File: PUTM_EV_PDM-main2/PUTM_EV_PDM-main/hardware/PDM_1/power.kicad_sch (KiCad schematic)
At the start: 20 parts, among them U2 LD1117S33TR_SOT223, U3 LM2675M-5

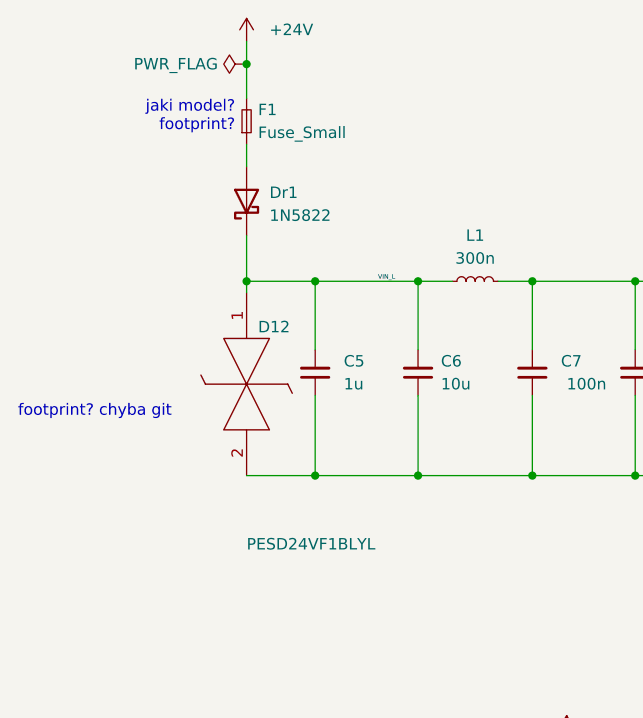
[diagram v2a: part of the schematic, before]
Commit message: małe zmiany
dodano złącza
zmieniono parę footprintów
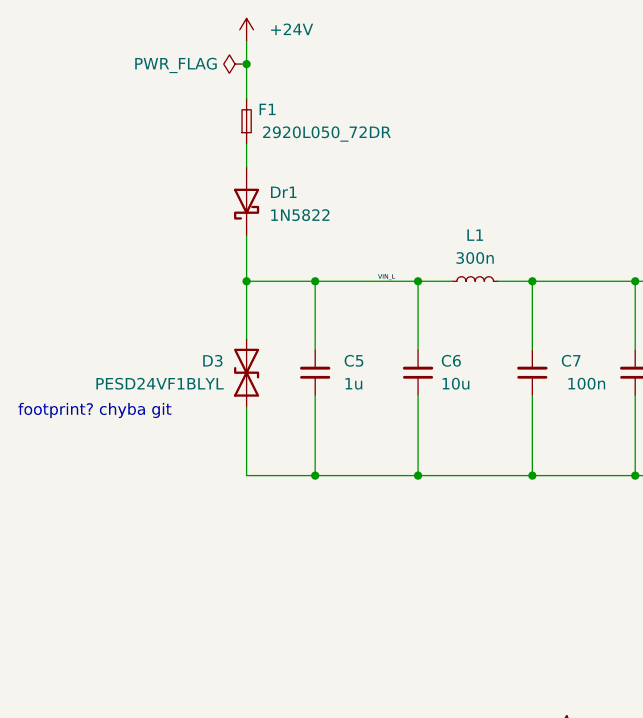
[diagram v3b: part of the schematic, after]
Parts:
- removed D12: PESD24VF1BLYL, Diode_SMD:D_SMA, symbol PESD24VF1BLYL:PESD24VF1BLYL
- added D3: PESD24VF1BLYL, Diode_SMD:D_SMA, symbol Device:D_TVS
- C14: footprint Capacitor_SMD:CP_Elec_6.3x5.5 -> Capacitor_SMD:CP_Elec_6.3x5.4
- F1: value Fuse_Small -> 2920L050_72DR; footprint (none) -> FUSC7451X125N; Height (none) -> 1.25; Manufacturer_Name (none) -> LITTELFUSE; Manufacturer_Part_Number (none) -> 2920L050/72DR; Mouser Part Number (none) -> 576-2920L050/72DR; Mouser Price/Stock (none) -> https://www.mouser.co.uk/ProductDetail/Littelfuse/2920L050-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
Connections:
- net GND: now also D3.1 (A1)
- net VIN_L: now also D3.2 (A2)
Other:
- note removed: "jaki model? footprint?"
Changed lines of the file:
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@@
     (stroke (width 0) (type default))
   )
-  (wire (pts (xy 76.2 77.47) (xy 76.2 78.74))
+  (wire (pts (xy 76.2 77.47) (xy 76.2 83.82))
     (stroke (width 0) (type default))
   )
   (wire (pts (xy 119.38 77.47) (xy 129.54 77.47))
+    (stroke (width 0) (type default))
+  )
+  (wire (pts (xy 76.2 91.44) (xy 76.2 99.06))
     (stroke (width 0) (type default))
   )
@@
   (text "footprint? chyba git" (at 50.8 92.71 0)
     (effects (font (size 1.27 1.27)) (justify left bottom))
-  )
-  (text "jaki model?\nfootprint?\n" (at 74.93 60.96 0)
-    (effects (font (size 1.27 1.27)) (justify right bottom))
   )
   (text "5v to 3.3V" (at 147.955 118.11 0)
@@
     )
   )
-  (symbol (lib_id "PESD24VF1BLYL:PESD24VF1BLYL") (at 76.2 78.74 270) (unit 1)
-    (in_bom yes) (on_board yes) (dnp no)
-    (property "Reference" "D12" (at 77.47 82.55 90)
-      (effects (font (size 1.27 1.27)) (justify left))
-    )
-    (property "Value" "PESD24VF1BLYL" (at 76.2 106.68 90)
-      (effects (font (size 1.27 1.27)) (justify left))
-    )
-    (property "Footprint" "Diode_SMD:D_SMA" (at 80.01 93.98 0)
-      (effects (font (size 1.27 1.27)) (justify left bottom) hide)
-    )
-    (property "Datasheet" "https://assets.nexperia.com/documents/data-sheet/PESD24VF1BL.pdf" (at 77.47 93.98 0)
-      (effects (font (size 1.27 1.27)) (justify left bottom) hide)
-    )
-    (property "Description" "PESD24VF1BL - Ultra low capacitance bidirectional ESD protection diode" (at 74.93 93.98 0)
-      (effects (font (size 1.27 1.27)) (justify left bottom) hide)
-    )
-    (property "Height" "0" (at 72.39 93.98 0)
-      (effects (font (size 1.27 1.27)) (justify left bottom) hide)
-    )
-    (property "Mouser Part Number" "771-PESD24VF1BLYL" (at 69.85 93.98 0)
-      (effects (font (size 1.27 1.27)) (justify left bottom) hide)
-    )
-    (property "Mouser Price/Stock" "https://www.mouser.co.uk/ProductDetail/Nexperia/PESD24VF1BLYL?qs=M%2FOdCRO8QQ2u4QQQVkgemw%3D%3D" (at 67.31 93.98 0)
-      (effects (font (size 1.27 1.27)) (justify left bottom) hide)
-    )
-    (property "Manufacturer_Name" "Nexperia" (at 64.77 93.98 0)
-      (effects (font (size 1.27 1.27)) (justify left bottom) hide)
-    )
-    (property "Manufacturer_Part_Number" "PESD24VF1BLYL" (at 62.23 93.98 0)
-      (effects (font (size 1.27 1.27)) (justify left bottom) hide)
-    )
-    (pin "1")
-    (pin "2")
-    (instances
-      (project "PDM_1"
-        (path "/b652b05a-4e3d-4ad1-b032-18886abe7d45/1367ec17-5fee-46da-adec-17b799499894"
-          (reference "D12") (unit 1)
-        )
-      )
-    )
-  )
   (symbol (lib_id "Device:L_Small") (at 101.6 77.47 90) (unit 1)
     (in_bom yes) (on_board yes) (dnp no) (fields_autoplaced)
@@
       (effects (font (size 1.27 1.27)) (justify left))
     )
-    (property "Footprint" "Capacitor_SMD:CP_Elec_6.3x5.5" (at 203.2 93.98 0)
+    (property "Footprint" "Capacitor_SMD:CP_Elec_6.3x5.4" (at 203.2 93.98 0)
       (effects (font (size 1.27 1.27)) hide)
     )
@@
     )
   )
+  (symbol (lib_id "Device:D_TVS") (at 76.2 87.63 90) (unit 1)
+    (in_bom yes) (on_board yes) (dnp no)
+    (property "Reference" "D3" (at 73.66 86.36 90)
+      (effects (font (size 1.27 1.27)) (justify left))
+    )
+    (property "Value" "PESD24VF1BLYL" (at 73.66 88.9 90)
+      (effects (font (size 1.27 1.27)) (justify left))
+    )
+    (property "Footprint" "Diode_SMD:D_SMA" (at 76.2 87.63 0)
+      (effects (font (size 1.27 1.27)) hide)
+    )
+    (property "Datasheet" "https://assets.nexperia.com/documents/data-sheet/PESD24VF1BL.pdf" (at 76.2 87.63 0)
+      (effects (font (size 1.27 1.27)) hide)
+    )
+    (property "description" "PESD24VF1BL - Ultra low capacitance bidirectional ESD protection diode" (at 76.2 87.63 90)
+      (effects (font (size 1.27 1.27)) hide)
+    )
+    (property "Mouser Part Number" "771-PESD24VF1BLYL" (at 76.2 87.63 90)
+      (effects (font (size 1.27 1.27)) (justify left bottom) hide)
+    )
+    (property "Mouser Price/Stock" "https://www.mouser.co.uk/ProductDetail/Nexperia/PESD24VF1BLYL?qs=M%2FOdCRO8QQ2u4QQQVkgemw%3D%3D" (at 76.2 87.63 90)
+      (effects (font (size 1.27 1.27)) (justify left bottom) hide)
+    )
+    (property "Manufacturer_Part_Number" "PESD24VF1BLYL" (at 76.2 87.63 90)
+      (effects (font (size 1.27 1.27)) (justify left bottom) hide)
+    )
+    (pin "1")
+    (pin "2")
+    (instances
+      (project "PDM_1"
+        (path "/b652b05a-4e3d-4ad1-b032-18886abe7d45/1367ec17-5fee-46da-adec-17b799499894"
+          (reference "D3") (unit 1)
+        )
+      )
+    )
+  )
   (symbol (lib_id "Device:Fuse_Small") (at 76.2 59.69 90) (unit 1)
-    (in_bom yes) (on_board yes) (dnp no) (fields_autoplaced)
+    (in_bom yes) (on_board yes) (dnp no)
     (property "Reference" "F1" (at 77.47 58.42 90)
       (effects (font (size 1.27 1.27)) (justify right))
     )
-    (property "Value" "Fuse_Small" (at 77.47 60.96 90)
-      (effects (font (size 1.27 1.27)) (justify right))
-    )
-    (property "Footprint" "" (at 76.2 59.69 0)
-      (effects (font (size 1.27 1.27)) hide)
-    )
-    (property "Datasheet" "~" (at 76.2 59.69 0)
-      (effects (font (size 1.27 1.27)) hide)
-    )
-    (pin "2")
+    (property "Value" "2920L050_72DR" (at 85.09 60.96 90)
+      (effects (font (size 1.27 1.27)))
+    )
+    (property "Footprint" "FUSC7451X125N" (at 76.2 59.69 0)
+      (effects (font (size 1.27 1.27)) (justify left top) hide)
+    )
+    (property "Datasheet" "https://www.littelfuse.com/media?resourcetype=datasheets&itemid=f237e8c2-1ed9-4c13-a738-dbe0738b3d2c&filename=2920l-datasheet-update" (at 76.2 59.69 0)
+      (effects (font (size 1.27 1.27)) (justify left top) hide)
+    )
+    (property "Height" "1.25" (at 76.2 59.69 90)
+      (effects (font (size 1.27 1.27)) (justify right bottom) hide)
+    )
+    (property "Mouser Part Number" "576-2920L050/72DR" (at 76.2 59.69 90)
+      (effects (font (size 1.27 1.27)) (justify right bottom) hide)
+    )
+    (property "Mouser Price/Stock" "https://www.mouser.co.uk/ProductDetail/Littelfuse/2920L050-72DR?qs=ST9lo4GX8V0DAh6PAk7A0Q%3D%3D" (at 76.2 59.69 90)
+      (effects (font (size 1.27 1.27)) (justify right bottom) hide)
+    )
+    (property "Manufacturer_Name" "LITTELFUSE" (at 76.2 59.69 90)
+      (effects (font (size 1.27 1.27)) (justify right bottom) hide)
+    )
+    (property "Manufacturer_Part_Number" "2920L050/72DR" (at 76.2 59.69 90)
+      (effects (font (size 1.27 1.27)) (justify right bottom) hide)
+    )
+    (pin "2")
